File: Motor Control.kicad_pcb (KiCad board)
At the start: 2 copper layers, 160 x 135.3 mm, 118 parts, among them J1 Conn_01x02_Socket, J4 Conn_01x02_Socket, J400 Conn_01x05_Pin, J410 Conn_01x06_Pin, J411 USB_B, J5 Conn_01x02_Socket, J6 Conn_01x02_Socket, Q110 IRLZ44N, Q111 BC557, Q112 BC547, Q113 BC557, Q120 IRLZ44N, Q121 BC557, Q122 BC547, Q123 BC557, Q130 IRLZ44N, Q131 BC547, Q132 BC557, Q140 IRLZ44N, Q141 BC547, Q142 BC557, Q210 BC547, Q220 BC547, Q230 BC547, Q240 BC547, SW310 RotaryEncoder_Switch_MP, U210 4N35, U220 4N35, U230 4N35, U240 4N35, U300 74AHC595, U400 PIC18F26K22-xSP, U410 MCP2221AxP, U900 LM317, U901 L78L05_TO92, U902 HCPL7510

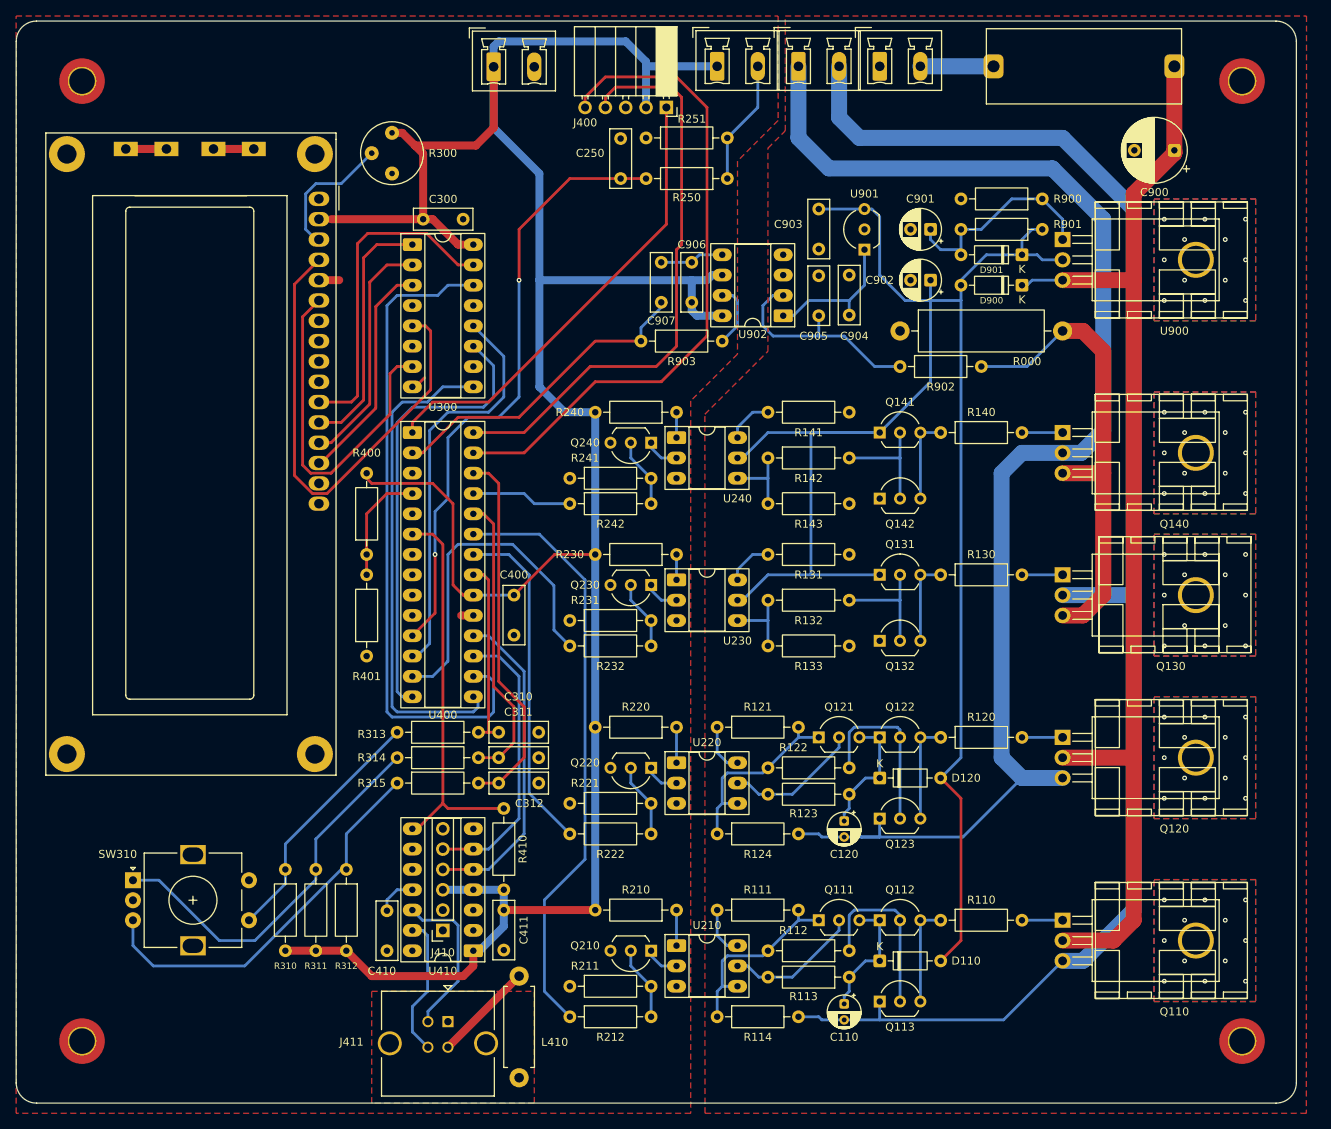
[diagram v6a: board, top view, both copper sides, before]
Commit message: V 1.0.1
Stiched vias under TO 220
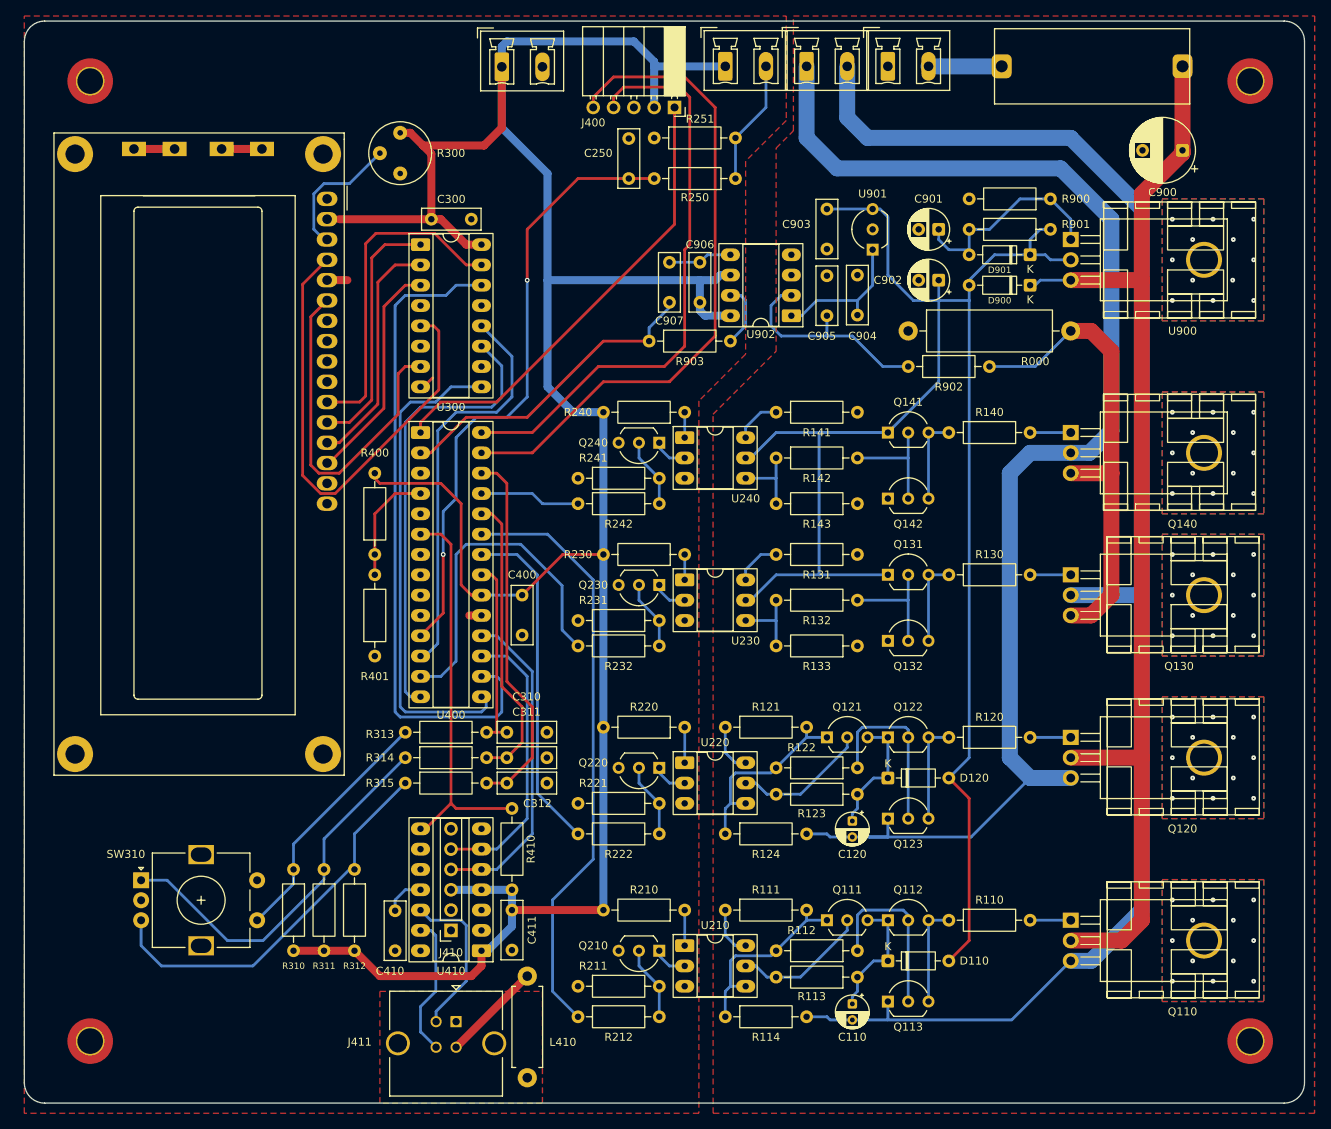
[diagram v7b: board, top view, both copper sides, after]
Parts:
- moved REF** 1.49 mm to (200.2, 117.6)
- moved REF** 1.49 mm to (200.2, 140.5)
- moved C110 1.02 mm to (168.3, 141.3)
- moved C120 1.02 mm to (168.3, 118.4)
- moved C250 1.02 mm to (140.3, 38.1)
- moved C300 1.02 mm to (115.7, 43.2)
- moved C411 1.02 mm to (125.7, 129.5)
- moved C900 1.02 mm to (209.6, 34.6)
- moved C904 1.02 mm to (168.9, 55.2)
- moved D110 1.02 mm to (172.7, 135.9)
- moved D120 1.02 mm to (172.7, 113.0)
- moved D900 1.02 mm to (190.5, 51.4)
- moved D901 1.02 mm to (190.5, 47.6)
- moved DS300 1.02 mm to (68.5, 112.7)
- moved J4 1.02 mm to (162.6, 24.1)
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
